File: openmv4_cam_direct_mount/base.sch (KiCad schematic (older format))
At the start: 63 parts, among them M1 9774030243R, M2 9774030243R, Q1 BSS138, Q2 Si2301BDS, U1 STM32H743VIT6, U2 OV7725, U5 TPS731XX, U8 PAM2305AABADJ, X1 MF-CON-MICROUSB-RIGHT, X2 USD-1040310811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

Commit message: Changes to KiCAD
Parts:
- removed M1, M2: 9774030243R, base:9774030151R, symbol base-eagle-import:9774030151R
- U2: footprint (none) -> openmv3:CSP2-28
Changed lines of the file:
@@
-$EndComp
-$Comp
-L base-eagle-import:DINA3_L #FRAME1
-U 2 1 CC96BE8F
-P 15100 12900
-F 0 "#FRAME1" H 15100 12900 50  0001 C CNN
-F 1 "DINA3_L" H 15100 12900 50  0001 C CNN
-F 2 "" H 15100 12900 50  0001 C CNN
-F 3 "" H 15100 12900 50  0001 C CNN
-	2    15100 12900
-	1    0    0    -1
 $EndComp
 $Comp
@@
 F 3 "" H 18000 5200 50  0001 C CNN
 	1    18000 5200
-	1    0    0    -1
-$EndComp
-$Comp
-L base-eagle-import:9774030151R M1
-U 1 1 6705D9E8
-P 15800 11800
-F 0 "M1" H 15800 11800 50  0001 C CNN
-F 1 "9774030243R" H 15800 11800 50  0001 C CNN
-F 2 "base:9774030151R" H 15800 11800 50  0001 C CNN
-F 3 "" H 15800 11800 50  0001 C CNN
-	1    15800 11800
-	1    0    0    -1
-$EndComp
-$Comp
-L base-eagle-import:9774030151R M2
-U 1 1 29680FAA
-P 15300 11800
-F 0 "M2" H 15300 11800 50  0001 C CNN
-F 1 "9774030243R" H 15300 11800 50  0001 C CNN
-F 2 "base:9774030151R" H 15300 11800 50  0001 C CNN
-F 3 "" H 15300 11800 50  0001 C CNN
-	1    15300 11800
 	1    0    0    -1
 $EndComp
@@
 F 0 "U2" H 14550 10689 127 0000 C CNN
 F 1 "OV7725" H 14550 10482 127 0000 C CNN
-F 2 "" H 14550 9150 50  0001 C CNN
+F 2 "openmv3:CSP2-28" H 14550 9150 50  0001 C CNN
 F 3 "" H 14550 9150 50  0001 C CNN
 	1    14550 9150
@@
 	1    0    0    -1
 $EndComp
+$Comp
+L base-eagle-import:DINA3_L #FRAME1
+U 2 1 CC96BE8F
+P 15100 12900
+F 0 "#FRAME1" H 15100 12900 50  0001 C CNN
+F 1 "DINA3_L" H 15100 12900 50  0001 C CNN
+F 2 "" H 15100 12900 50  0001 C CNN
+F 3 "" H 15100 12900 50  0001 C CNN
+	2    15100 12900
+	1    0    0    -1
+$EndComp

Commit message: Fixed cam position
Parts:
- removed JP1, JP2: PINHD-1X8, base:1X08, symbol base-eagle-import:PINHD-1X8
- removed X4: S2B-PH-K-S(LF)(SN), base:JST-PH-2-THM-RA, symbol base-eagle-import:JST_2PIN-THM-RA
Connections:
- wire segments 332 -> 309
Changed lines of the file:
@@
-GND
-Wire Wire Line
-	13000 2900 11500 2900
-Wire Wire Line
-	13000 2600 11500 2600
-Wire Wire Line
-	11500 2600 11500 2900
-Wire Wire Line
-	11500 2900 11500 3100
-Connection ~ 11500 2900
-Text Label 13000 2900 0    10   ~ 0
 GND
 Wire Wire Line
@@
 NRST
 Wire Wire Line
-	13000 1900 11600 1900
-Text Label 11600 1900 0    70   ~ 0
-NRST
-Wire Wire Line
 	3500 8200 2800 8200
 Text Label 2800 8200 0    70   ~ 0
@@
 	1800 6400 1800 6800
 Text Label 3000 6400 0    70   ~ 0
-BOOT0
-Wire Wire Line
-	13000 2000 11600 2000
-Text Label 11600 2000 0    70   ~ 0
 BOOT0
 Wire Wire Line
@@
 VCC
 Wire Wire Line
-	15000 2600 13500 2600
-Wire Wire Line
-	13500 2600 13500 1700
-Text Label 15000 2600 0    10   ~ 0
-VCC
-Wire Wire Line
 	14200 6000 14300 6000
 Wire Wire Line
@@
 LED_R
 Wire Wire Line
-	13000 2400 11600 2400
-Text Label 11600 2400 0    70   ~ 0
-TIM4_CH1
-Wire Wire Line
 	9000 8100 9800 8100
 Text Label 9300 8100 0    70   ~ 0
 TIM4_CH1
 Wire Wire Line
-	13000 2300 11600 2300
-Text Label 11600 2300 0    70   ~ 0
-TIM4_CH2
-Wire Wire Line
 	9000 8200 9800 8200
 Text Label 9300 8200 0    70   ~ 0
@@
 SPI2_SCLK
 Wire Wire Line
-	13600 2100 15000 2100
-Text Label 13600 2100 0    70   ~ 0
-SPI2_SCLK
-Wire Wire Line
 	3500 9700 2800 9700
 Text Label 2800 9700 0    70   ~ 0
 I2C2_SCL
 Wire Wire Line
-	15000 2300 13600 2300
-Text Label 13600 2300 0    70   ~ 0
-I2C2_SCL
-Wire Wire Line
 	3500 9800 2800 9800
 Text Label 2800 9800 0    70   ~ 0
-I2C2_SDA
-Wire Wire Line
-	15000 2400 13600 2400
-Text Label 13600 2400 0    70   ~ 0
 I2C2_SDA
 Wire Wire Line
@@
 DAC
 Wire Wire Line
-	15000 2500 13600 2500
-Text Label 13600 2500 0    70   ~ 0
-DAC
-Wire Wire Line
 	3500 9900 2800 9900
 Text Label 2800 9900 0    70   ~ 0
 SPI2_NSS
 Wire Wire Line
-	13600 2200 15000 2200
-Text Label 13600 2200 0    70   ~ 0
-SPI2_NSS
-Wire Wire Line
 	3500 10100 2800 10100
 Text Label 2800 10100 0    70   ~ 0
 SPI2_MISO
 Wire Wire Line
-	13600 2000 15000 2000
-Text Label 13600 2000 0    70   ~ 0
-SPI2_MISO
-Wire Wire Line
 	3500 10200 2800 10200
 Text Label 2800 10200 0    70   ~ 0
 SPI2_MOSI
 Wire Wire Line
-	13600 1900 15000 1900
-Text Label 13600 1900 0    70   ~ 0
-SPI2_MOSI
-Wire Wire Line
 	9000 7800 9800 7800
 Text Label 9300 7800 0    70   ~ 0
@@
 	9000 8300 9800 8300
 Text Label 9300 8300 0    70   ~ 0
-TIM4_CH3
-Wire Wire Line
-	13000 2200 11600 2200
-Text Label 11600 2200 0    70   ~ 0
 TIM4_CH3
 Wire Wire Line
@@
 VIN
 Wire Wire Line
-	13000 3000 11400 3000
-Wire Wire Line
-	11400 3000 11400 2500
-Wire Wire Line
-	13000 2500 11400 2500
-Wire Wire Line
-	11400 2500 11400 1700
-Text Label 11600 2500 0    70   ~ 0
-VIN
-Connection ~ 11400 2500
-Wire Wire Line
 	1600 2200 1900 2200
 Wire Wire Line
 	6800 1900 6900 1900
-Wire Wire Line
-	13000 2100 11600 2100
-Text Label 11600 2100 0    70   ~ 0
-DCMI_FSIN
 Text Label 19350 8650 0    70   ~ 0
 DCMI_FSIN
@@
 $EndComp
 $Comp
-L base-eagle-import:PINHD-1X8 JP2
-U 1 1 BAFA783C
-P 13100 2300
-F 0 "JP2" H 12850 2825 59  0000 L BNN
-F 1 "PINHD-1X8" H 12850 1800 59  0000 L BNN
-F 2 "base:1X08" H 13100 2300 50  0001 C CNN
-F 3 "" H 13100 2300 50  0001 C CNN
-	1    13100 2300
-	1    0    0    -1
-$EndComp
-$Comp
-L base-eagle-import:PINHD-1X8 JP1
-U 1 1 0B60073D
-P 15100 2300
-F 0 "JP1" H 14850 2825 59  0000 L BNN
-F 1 "PINHD-1X8" H 14850 1800 59  0000 L BNN
-F 2 "base:1X08" H 15100 2300 50  0001 C CNN
-F 3 "" H 15100 2300 50  0001 C CNN
-	1    15100 2300
-	1    0    0    -1
-$EndComp
-$Comp
-L base-eagle-import:GND #GND05
-U 1 1 5B6A58CA
-P 11500 3200
-F 0 "#GND05" H 11500 3200 50  0001 C CNN
-F 1 "GND" H 11400 3100 59  0000 L BNN
-F 2 "" H 11500 3200 50  0001 C CNN
-F 3 "" H 11500 3200 50  0001 C CNN
-	1    11500 3200
-	1    0    0    -1
-$EndComp
-$Comp
 L base-eagle-import:VCC #P+02
 U 1 1 637B3A6A
@@
 F 3 "" H 13000 6000 50  0001 C CNN
 	1    13000 6000
-	1    0    0    -1
-$EndComp
-$Comp
-L base-eagle-import:VCC #P+06
-U 1 1 4B6CF0C8
-P 13500 1700
-F 0 "#P+06" H 13500 1700 50  0001 C CNN
-F 1 "VCC" V 13400 1600 59  0000 L BNN
-F 2 "" H 13500 1700 50  0001 C CNN
-F 3 "" H 13500 1700 50  0001 C CNN
-	1    13500 1700
 	1    0    0    -1
 $EndComp
@@
 	1    0    0    -1
 $EndComp
-$Comp
-L base-eagle-import:JST_2PIN-THM-RA X4
-U 1 1 BE05CED0
-P 13100 3000
-F 0 "X4" H 12850 3225 59  0000 L BNN
-F 1 "S2B-PH-K-S(LF)(SN)" H 12850 2800 59  0000 L BNN
-F 2 "base:JST-PH-2-THM-RA" H 13100 3000 50  0001 C CNN
-F 3 "" H 13100 3000 50  0001 C CNN
-	1    13100 3000
-	1    0    0    -1
-$EndComp
-$Comp
-L base-eagle-import:VIN #VIN03
-U 1 1 73E98C85
-P 11400 1700
-F 0 "#VIN03" H 11400 1700 50  0001 C CNN
-F 1 "VIN" V 11300 1600 59  0000 L BNN
-F 2 "" H 11400 1700 50  0001 C CNN
-F 3 "" H 11400 1700 50  0001 C CNN
-	1    11400 1700
-	1    0    0    -1
-$EndComp

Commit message: Connecting key components
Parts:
- removed C14: 47uF, base:EIA3216, symbol base-eagle-import:CAP_POL1206
- C12: renamed from C16; footprint base:EIA3216 -> openmv3:EIA3216
- C15: renamed from C20; footprint base:0603-CAP -> openmv3:0603-CAP
- C16: renamed from C22; footprint base:0603-CAP -> openmv3:0603-CAP
- C17: renamed from C21; footprint base:0603-CAP -> openmv3:0603-CAP
- C19: renamed from C17; footprint base:0603-CAP -> openmv3:0603-CAP
- C20: renamed from C18; footprint base:0603-CAP -> openmv3:0805
- R4: renamed from R6; footprint base:0603-RES -> openmv3:0603-RES
- RN4A1: renamed from R4; footprint base:0603-RES -> openmv3:EXBV4V
- RN4B1: renamed from R3; footprint base:0603-RES -> openmv3:EXBV4V
- renumbered C19 to C18, C15 to C21, C12 to C22, R11 to R3
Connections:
- net labels removed: RSVD1, RSVD2, RSVD3, RSVD4, RSVD5, RSVD6
- wire segments 309 -> 305
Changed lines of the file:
@@
-GND
-Wire Wire Line
-	18500 9850 18500 8750
-Text Label 18500 9850 0    10   ~ 0
 GND
 Wire Wire Line
@@
 	10200 2900 10200 3100
 Text Label 10200 2900 0    10   ~ 0
-GND
-Text Label 19350 8450 0    70   ~ 0
-GND
-Text Label 19350 8850 0    70   ~ 0
-GND
-Text Label 19350 7750 0    70   ~ 0
 GND
 Wire Wire Line
@@
 VCC
 Wire Wire Line
-	18500 7550 18500 7650
-Text Label 18500 7550 0    10   ~ 0
-VCC
-Wire Wire Line
 	8600 2100 8600 2000
 Wire Wire Line
@@
 Text Label 9300 5800 0    70   ~ 0
 DCMI_D0
-Text Label 19350 9050 0    70   ~ 0
-DCMI_D0
 Wire Wire Line
 	9000 5900 9700 5900
 Text Label 9300 5900 0    70   ~ 0
 DCMI_D1
-Text Label 19350 8950 0    70   ~ 0
-DCMI_D1
 Wire Wire Line
 	3500 7500 2800 7500
@@
 Text Label 2800 7900 0    70   ~ 0
 DCMI_RST
-Text Label 19350 8550 0    70   ~ 0
-DCMI_RST
-Text Label 19350 8750 0    70   ~ 0
-DCMI_PWDN
 Wire Wire Line
 	9000 7600 9800 7600
@@
 Text Label 9300 8700 0    70   ~ 0
 DCMI_D2
-Text Label 19350 9250 0    70   ~ 0
-DCMI_D2
 Wire Wire Line
 	9000 8800 9800 8800
@@
 Text Label 2800 9300 0    70   ~ 0
 DCMI_D5
-Text Label 19350 9150 0    70   ~ 0
-DCMI_D5
 Wire Wire Line
 	9000 9200 9800 9200
@@
 Text Label 9300 5200 0    70   ~ 0
 LED_R
-Wire Wire Line
-	9000 8100 9800 8100
-Text Label 9300 8100 0    70   ~ 0
-TIM4_CH1
-Wire Wire Line
-	9000 8200 9800 8200
-Text Label 9300 8200 0    70   ~ 0
-TIM4_CH2
 Wire Wire Line
 	17500 5400 16900 5400
@@
 	13900 6000 13700 6000
 Wire Wire Line
-	9000 8300 9800 8300
-Text Label 9300 8300 0    70   ~ 0
-TIM4_CH3
-Wire Wire Line
 	12400 4600 12800 4600
 Wire Wire Line
@@
 Wire Wire Line
 	6800 1900 6900 1900
-Text Label 19350 8650 0    70   ~ 0
-DCMI_FSIN
 Wire Wire Line
 	9000 7400 9800 7400
@@
 Text Label 2800 9100 0    70   ~ 0
 SPI3_MISO
-Text Label 19350 8250 0    70   ~ 0
-SPI3_MISO
 Wire Wire Line
 	3500 9200 2800 9200
 Text Label 2800 9200 0    70   ~ 0
 SPI3_MOSI
-Text Label 19350 8350 0    70   ~ 0
-SPI3_MOSI
 Wire Wire Line
 	9000 7200 9800 7200
@@
 Text Label 9300 7300 0    70   ~ 0
 GPIO2
-Text Label 19350 8050 0    70   ~ 0
-SPI3_SSEL
 Wire Wire Line
 	3500 8400 2800 8400
@@
 Text Label 10500 1700 0    10   ~ 0
 VDDA
-Wire Wire Line
-	19000 8200 19000 7700
-Text Label 19350 7550 0    70   ~ 0
-RSVD1
-Text Label 19350 7650 0    70   ~ 0
-RSVD2
-Text Label 19350 7850 0    70   ~ 0
-RSVD3
-Text Label 19350 7950 0    70   ~ 0
-RSVD4
 Wire Wire Line
 	6800 2500 7500 2500
@@
 $EndComp
 $Comp
-L base-eagle-import:VCC #P+05
-U 1 1 57F4DC09
-P 18500 7550
-F 0 "#P+05" H 18500 7550 50  0001 C CNN
-F 1 "VCC" V 18600 7350 59  0000 L BNN
-F 2 "" H 18500 7550 50  0001 C CNN
-F 3 "" H 18500 7550 50  0001 C CNN
-	1    18500 7550
-	-1   0    0    -1
-$EndComp
-$Comp
 L base-eagle-import:USD-1040310811 X2
 U 1 1 EE6A8C5B
@@
 	1    18000 5200
 	1    0    0    -1
-$EndComp
-$Comp
-L base-eagle-import:GND #GND04
-U 1 1 12C122FD
-P 18500 9950
-F 0 "#GND04" H 18500 9950 50  0001 C CNN
-F 1 "GND" H 18400 9850 59  0000 L BNN
-F 2 "" H 18500 9950 50  0001 C CNN
-F 3 "" H 18500 9950 50  0001 C CNN
-	1    18500 9950
-	-1   0    0    -1
 $EndComp
 $Comp
@@
 $EndComp
 $Comp
-L base-eagle-import:CAP0805 C12
+L base-eagle-import:CAP0805 C22
 U 1 1 0AD37B5F
 P 10500 2200
-F 0 "C12" H 10560 2315 59  0000 L BNN
+F 0 "C22" H 10560 2315 59  0000 L BNN
 F 1 "10uF" H 10560 2115 59  0000 L BNN
 F 2 "base:0805" H 10500 2200 50  0001 C CNN
@@
 $EndComp
 $Comp
-L base-eagle-import:VDDA #VDDA02
-U 1 1 72A79A59
-P 19000 7700
-F 0 "#VDDA02" H 19000 7700 50  0001 C CNN
-F 1 "VDDA" V 18900 7500 59  0000 L BNN
-F 2 "" H 19000 7700 50  0001 C CNN
-F 3 "" H 19000 7700 50  0001 C CNN
-	1    19000 7700
-	1    0    0    -1
-$EndComp
-$Comp
-L base-eagle-import:CAP_POL1206 C14
-U 1 1 BF09C543
-P 18500 8550
-F 0 "C14" V 18475 8290 59  0000 L BNN
-F 1 "47uF" V 18590 8590 59  0000 L BNN
-F 2 "base:EIA3216" H 18500 8550 50  0001 C CNN
-F 3 "" H 18500 8550 50  0001 C CNN
-	1    18500 8550
-	1    0    0    -1
-$EndComp
-$Comp
-L base-eagle-import:CAP_POL1206 C15
+L base-eagle-import:CAP_POL1206 C21
 U 1 1 6CF7C31D
 P 16100 5800
-F 0 "C15" V 16075 5540 59  0000 L BNN
+F 0 "C21" V 16075 5540 59  0000 L BNN
 F 1 "47uF" V 16190 5840 59  0000 L BNN
 F 2 "base:EIA3216" H 16100 5800 50  0001 C CNN
@@
 Text Notes 15200 10700 0    100  ~ 20
 Notes:
-Text Notes 11450 7250 0    300  ~ 60
+Text Notes 11500 7200 0    300  ~ 60
 IMAGE SENSOR CONNECTOR
 Text Notes 900  3800 0    300  ~ 60
@@
 	1    0    0    -1
 $EndComp
-Connection ~ 18500 7650
-Wire Wire Line
-	18500 7650 18500 8450
 Wire Wire Line
 	15450 8050 16000 8050
@@
 	16500 8550 16800 8550
 $Comp
-L base-eagle-import:RESISTOR0603-RES R3
+L base-eagle-import:RESISTOR0603-RES RN4B1
 U 1 1 691E95C4
 P 16300 8550
-F 0 "R3" H 16400 8550 59  0000 L BNN
+F 0 "RN4B1" H 16400 8550 59  0000 L BNN
 F 1 "4.7K" H 16000 8550 59  0000 L BNN
-F 2 "base:0603-RES" H 16300 8550 50  0001 C CNN
+F 2 "openmv3:EXBV4V" H 16300 8550 50  0001 C CNN
 F 3 "" H 16300 8550 50  0001 C CNN
 	1    16300 8550
@@
 $EndComp
 $Comp
-L base-eagle-import:RESISTOR0603-RES R4
+L base-eagle-import:RESISTOR0603-RES RN4A1
 U 1 1 738A1E18
 P 16300 8750
-F 0 "R4" H 16400 8750 59  0000 L BNN
+F 0 "RN4A1" H 16400 8750 59  0000 L BNN
 F 1 "4.7K" H 16000 8750 59  0000 L BNN
-F 2 "base:0603-RES" H 16300 8750 50  0001 C CNN
+F 2 "openmv3:EXBV4V" H 16300 8750 50  0001 C CNN
 F 3 "" H 16300 8750 50  0001 C CNN
 	1    16300 8750
@@
 DCMI_D7
 $Comp
-L base-eagle-import:RESISTOR0603-RES R11
+L base-eagle-import:RESISTOR0603-RES R3
 U 1 1 5DDF9B60
 P 12900 9750
-F 0 "R11" H 13000 9650 59  0000 L BNN
+F 0 "R3" H 13000 9650 59  0000 L BNN
 F 1 "10K" H 12650 9650 59  0000 L BNN
 F 2 "base:0603-RES" H 12900 9750 50  0001 C CNN
@@
 	13550 9850 13550 10350
 $Comp
-L base-eagle-import:CAP0603-CAP C22
+L base-eagle-import:CAP0603-CAP C16
 U 1 1 5DF32C86
 P 13350 9900
-F 0 "C22" V 13425 9990 59  0000 L BNN
+F 0 "C16" V 13425 9990 59  0000 L BNN
 F 1 "0.1uF" V 13450 9650 59  0000 L BNN
-F 2 "base:0603-CAP" H 13350 9900 50  0001 C CNN
+F 2 "openmv3:0603-CAP" H 13350 9900 50  0001 C CNN
 F 3 "" H 13350 9900 50  0001 C CNN
 	1    13350 9900
@@
 	13350 9450 13650 9450
 $Comp
-L base-eagle-import:CAP0603-CAP C21
+L base-eagle-import:CAP0603-CAP C17
 U 1 1 5DF6915A
 P 13150 9900
-F 0 "C21" V 13225 9990 59  0000 L BNN
+F 0 "C17" V 13225 9990 59  0000 L BNN
 F 1 "0.1uF" V 13250 9650 59  0000 L BNN
-F 2 "base:0603-CAP" H 13150 9900 50  0001 C CNN
+F 2 "openmv3:0603-CAP" H 13150 9900 50  0001 C CNN
 F 3 "" H 13150 9900 50  0001 C CNN
 	1    13150 9900
@@
 Wire Notes Line
 	15100 11500 700  11500
-Text Label 17500 7900 0    70   ~ 0
-RSVD6
-Text Label 17500 7800 0    70   ~ 0
-RSVD5
-Text Label 17500 7700 0    70   ~ 0
-VDDA
-Text Label 17500 9200 0    70   ~ 0
-I2C1_SDA
-Text Label 17500 9100 0    70   ~ 0
-I2C1_SCL
-Text Label 17500 8600 0    70   ~ 0
-DCMI_D7
-Text Label 17500 8700 0    70   ~ 0
-DCMI_D6
-Text Label 17500 8800 0    70   ~ 0
-DCMI_D4
-Text Label 17500 8900 0    70   ~ 0
-DCMI_D3
-Text Label 17500 8300 0    70   ~ 0
-DCMI_VSYNC
-Text Label 17500 8400 0    70   ~ 0
-DCMI_HSYNC
-Text Label 17500 8000 0    70   ~ 0
-VCC
-Text Label 17500 7600 0    70   ~ 0
-VCC
-Text Label 17500 9300 0    70   ~ 0
-VCC
-Text Label 17500 9000 0    70   ~ 0
-VCC
-Text Label 17500 8500 0    70   ~ 0
-VCC
 Text Label 13250 8950 0    50   ~ 0
 DCMI_FSIN
@@
 DCMI_PWDN
 $Comp
-L base-eagle-import:CAP0603-CAP C20
+L base-eagle-import:CAP0603-CAP C15
 U 1 1 5E02C609
 P 12600 9900
-F 0 "C20" V 12675 9990 59  0000 L BNN
+F 0 "C15" V 12675 9990 59  0000 L BNN
 F 1 "0.1uF" V 12700 9650 59  0000 L BNN
-F 2 "base:0603-CAP" H 12600 9900 50  0001 C CNN
+F 2 "openmv3:0603-CAP" H 12600 9900 50  0001 C CNN
 F 3 "" H 12600 9900 50  0001 C CNN
 	1    12600 9900
@@
 $EndComp
 $Comp
-L base-eagle-import:CAP0603-CAP C19
+L base-eagle-import:CAP0603-CAP C18
 U 1 1 5E063F93
 P 12350 9900
-F 0 "C19" V 12425 9990 59  0000 L BNN
+F 0 "C18" V 12425 9990 59  0000 L BNN
 F 1 "4.7uF" V 12450 9650 59  0000 L BNN
 F 2 "base:0603-CAP" H 12350 9900 50  0001 C CNN
@@
 $EndComp
 $Comp
-L base-eagle-import:CAP0603-CAP C18
+L base-eagle-import:CAP0603-CAP C20
 U 1 1 5E064271
 P 12100 9900
-F 0 "C18" V 12175 9990 59  0000 L BNN
+F 0 "C20" V 12175 9990 59  0000 L BNN
 F 1 "22uF" V 12200 9650 59  0000 L BNN
-F 2 "base:0603-CAP" H 12100 9900 50  0001 C CNN
+F 2 "openmv3:0805" H 12100 9900 50  0001 C CNN
 F 3 "" H 12100 9900 50  0001 C CNN
 	1    12100 9900
@@
 $EndComp
 $Comp
-L base-eagle-import:CAP0603-CAP C17
+L base-eagle-import:CAP0603-CAP C19
 U 1 1 5E065313
 P 11850 9900
-F 0 "C17" V 11925 9990 59  0000 L BNN
+F 0 "C19" V 11925 9990 59  0000 L BNN
 F 1 "0.1uF" V 11950 9650 59  0000 L BNN
-F 2 "base:0603-CAP" H 11850 9900 50  0001 C CNN
+F 2 "openmv3:0603-CAP" H 11850 9900 50  0001 C CNN
 F 3 "" H 11850 9900 50  0001 C CNN
 	1    11850 9900
@@
 	11850 10350 11850 10000
 $Comp
-L base-eagle-import:RESISTOR0603-RES R6
+L base-eagle-import:RESISTOR0603-RES R4
 U 1 1 5E0BB5CC
 P 12350 7850
-F 0 "R6" H 12300 7700 59  0000 L BNN
+F 0 "R4" H 12300 7700 59  0000 L BNN
 F 1 "10K" H 12300 7950 59  0000 L BNN
-F 2 "base:0603-RES" H 12350 7850 50  0001 C CNN
+F 2 "openmv3:0603-RES" H 12350 7850 50  0001 C CNN
 F 3 "" H 12350 7850 50  0001 C CNN
 	1    12350 7850
@@
 $EndComp
 $Comp
-L base-eagle-import:CAP_POL1206 C16
+L base-eagle-import:CAP_POL1206 C12
 U 1 1 5E0FBA1D
 P 11600 9000
-F 0 "C16" V 11575 8740 59  0000 L BNN
+F 0 "C12" V 11575 8740 59  0000 L BNN
 F 1 "47uF" V 11690 9040 59  0000 L BNN
-F 2 "base:EIA3216" H 11600 9000 50  0001 C CNN
+F 2 "openmv3:EIA3216" H 11600 9000 50  0001 C CNN
 F 3 "" H 11600 9000 50  0001 C CNN
 	1    11600 9000
@@
 	1    0    0    -1
 $EndComp
+Text Label 9300 8300 0    70   ~ 0
+TIM4_CH3
+Wire Wire Line
+	9000 8300 9800 8300
+Text Label 9300 8200 0    70   ~ 0
+TIM4_CH2
+Wire Wire Line
+	9000 8200 9800 8200
+Text Label 9300 8100 0    70   ~ 0
+TIM4_CH1
+Wire Wire Line
+	9000 8100 9800 8100
 $EndSCHEMATC

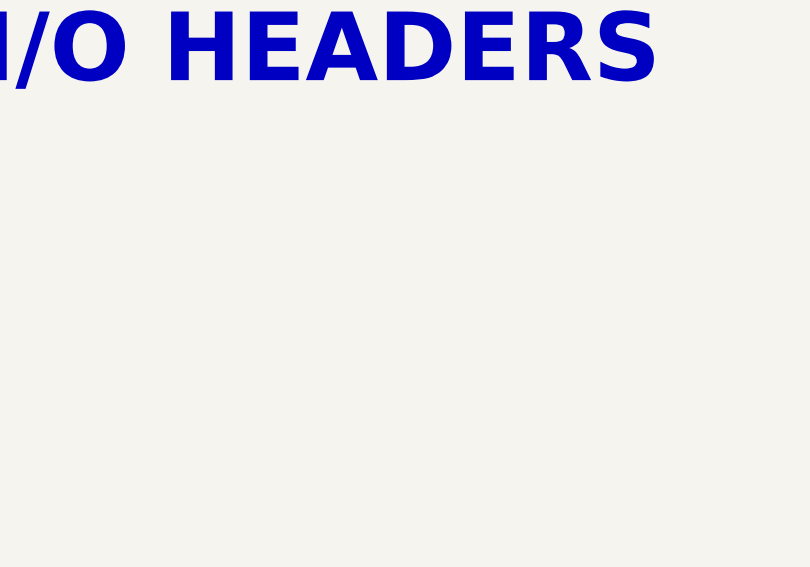
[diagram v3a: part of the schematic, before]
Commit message: Added connector to schematic
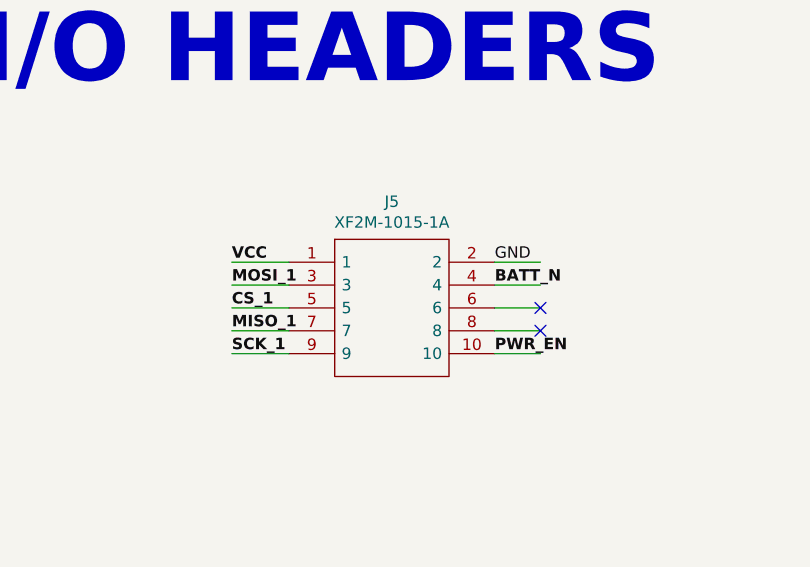
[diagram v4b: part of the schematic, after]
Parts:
- added J5: XF2M-1015-1A, XF2M-1015-1A, symbol XF2M-1015-1A:XF2M-1015-1A
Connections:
- net labels added: BATT_N, CS_1, MISO_1, MOSI_1, PWR_EN, SCK_1
- wire segments 305 -> 315
- no-connect marks 0 -> 2
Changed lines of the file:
@@
 Wire Wire Line
 	9000 8100 9800 8100
+$Comp
+L XF2M-1015-1A:XF2M-1015-1A J5
+U 1 1 5DBF5F14
+P 12750 1850
+F 0 "J5" H 13200 2115 50  0000 C CNN
+F 1 "XF2M-1015-1A" H 13200 2024 50  0000 C CNN
+F 2 "XF2M-1015-1A" H 13500 1950 50  0001 L CNN
+F 3 "https://componentsearchengine.com/Datasheets/3/XF2M-1015-1A.pdf" H 13500 1850 50  0001 L CNN
+F 4 "0.5mm Rotary backlock 10 way Omron XF2M Series 0.5mm Pitch 10 Way Right Angle SMT Female FPC Connector Locking Mechanism, Top and Bottom Contact" H 13500 1750 50  0001 L CNN "Description"
+F 5 "" H 13500 1650 50  0001 L CNN "Height"
+F 6 "Omron Electronics" H 13500 1550 50  0001 L CNN "Manufacturer_Name"
+F 7 "XF2M-1015-1A" H 13500 1450 50  0001 L CNN "Manufacturer_Part_Number"
+F 8 "653-XF2M-1015-1A" H 13500 1350 50  0001 L CNN "Mouser Part Number"
+F 9 "https://www.mouser.com/Search/Refine.aspx?Keyword=653-XF2M-1015-1A" H 13500 1250 50  0001 L CNN "Mouser Price/Stock"
+F 10 "7315772P" H 13500 1150 50  0001 L CNN "RS Part Number"
+F 11 "http://uk.rs-online.com/web/p/products/7315772P" H 13500 1050 50  0001 L CNN "RS Price/Stock"
+F 12 "70667825" H 13500 950 50  0001 L CNN "Allied_Number"
+F 13 "https://www.alliedelec.com/omron-electronic-components-xf2m-1015-1a/70667825/" H 13500 850 50  0001 L CNN "Allied Price/Stock"
+	1    12750 1850
+	1    0    0    -1
+$EndComp
+Text Label 13650 1850 0    50   ~ 0
+GND
+Wire Wire Line
+	13650 1850 13850 1850
+Wire Wire Line
+	13650 1950 13850 1950
+Wire Wire Line
+	13650 2050 13850 2050
+Wire Wire Line
+	13650 2150 13850 2150
+Wire Wire Line
+	13650 2250 13850 2250
+Wire Wire Line
+	12750 2250 12500 2250
+Wire Wire Line
+	12750 2150 12500 2150
+Wire Wire Line
+	12750 2050 12500 2050
+Wire Wire Line
+	12750 1950 12500 1950
+Wire Wire Line
+	12750 1850 12500 1850
+NoConn ~ 13850 2050
+NoConn ~ 13850 2150
+Text Label 13650 2250 0    50   ~ 10
+PWR_EN
+Text Label 12500 1850 0    50   ~ 10
+VCC
+Text Label 12500 1950 0    50   ~ 10
+MOSI_1
+Text Label 12500 2050 0    50   ~ 10
+CS_1
+Text Label 12500 2150 0    50   ~ 10
+MISO_1
+Text Label 12500 2250 0    50   ~ 10
+SCK_1
+Text Label 13650 1950 0    50   ~ 10
+BATT_N
 $EndSCHEMATC
